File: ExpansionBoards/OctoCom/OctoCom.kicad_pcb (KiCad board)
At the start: 4 copper layers, 106.7 x 83.8 mm, 101 parts, among them J1 Conn_02x10_Odd_Even, J10 Conn_02x02_Odd_Even, J11 Conn_02x02_Odd_Even, J12 Conn_02x02_Odd_Even, J13 Conn_02x02_Odd_Even, J14 DPD-09-11-B3, J15 Conn_02x02_Odd_Even, J16 Conn_02x02_Odd_Even, J17 Conn_02x02_Odd_Even, J18 Conn_02x02_Odd_Even, J19 Conn_02x02_Odd_Even, J2 Conn_02x20_Odd_Even, J20 Conn_02x02_Odd_Even, J21 DPD-09-11-B3, J22 Conn_02x02_Odd_Even, J23 Conn_02x02_Odd_Even, J24 Conn_02x02_Odd_Even, J25 Conn_02x02_Odd_Even, J26 Conn_02x02_Odd_Even, J27 Conn_02x02_Odd_Even, J28 DPD-09-11-B3, J29 Conn_02x02_Odd_Even, J30 Conn_02x02_Odd_Even, J31 Conn_02x02_Odd_Even, J32 Conn_02x04_Odd_Even, J33 4-171826-4, J34 Conn_02x03_Odd_Even, J4 DPD-09-11-B3, J5 Conn_02x02_Odd_Even, J6 Conn_02x02_Odd_Even, J7 Conn_02x02_Odd_Even, J8 Conn_02x02_Odd_Even, J9 Conn_02x02_Odd_Even, U1 ST16C554D, U10 SP3243EEY, U11 SP3243EEY, U12 74LS74, U14 SP3243EEY, U16 74LS00, U2 74LS139, U3 74HCT138, U4 SP3243EEY, U5 SP3243EEY, U6 SP3243EEY, U7 SP3243EEY, U8 SP3243EEY, U9 ST16C554D, X1 1.8432M, X1-ALT 1.8432M

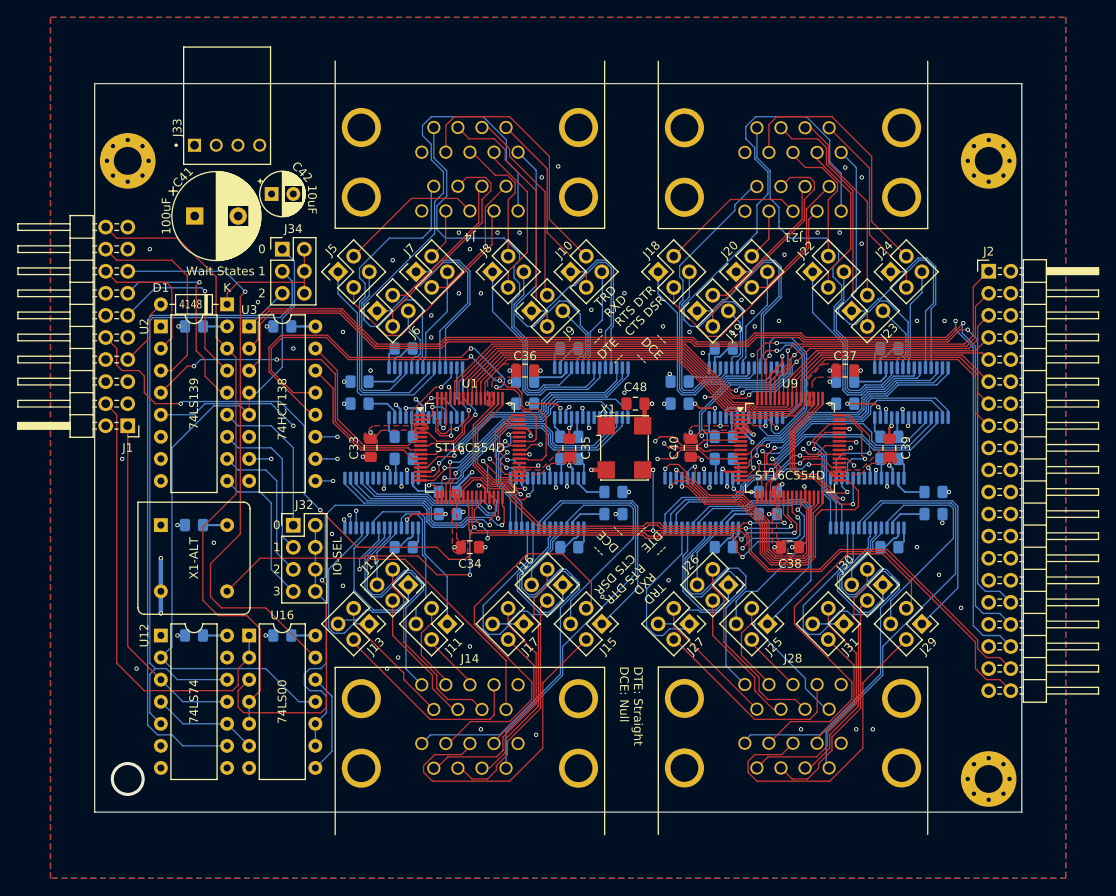
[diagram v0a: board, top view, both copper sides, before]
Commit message: rework octocom logic to use 22V10 for speed
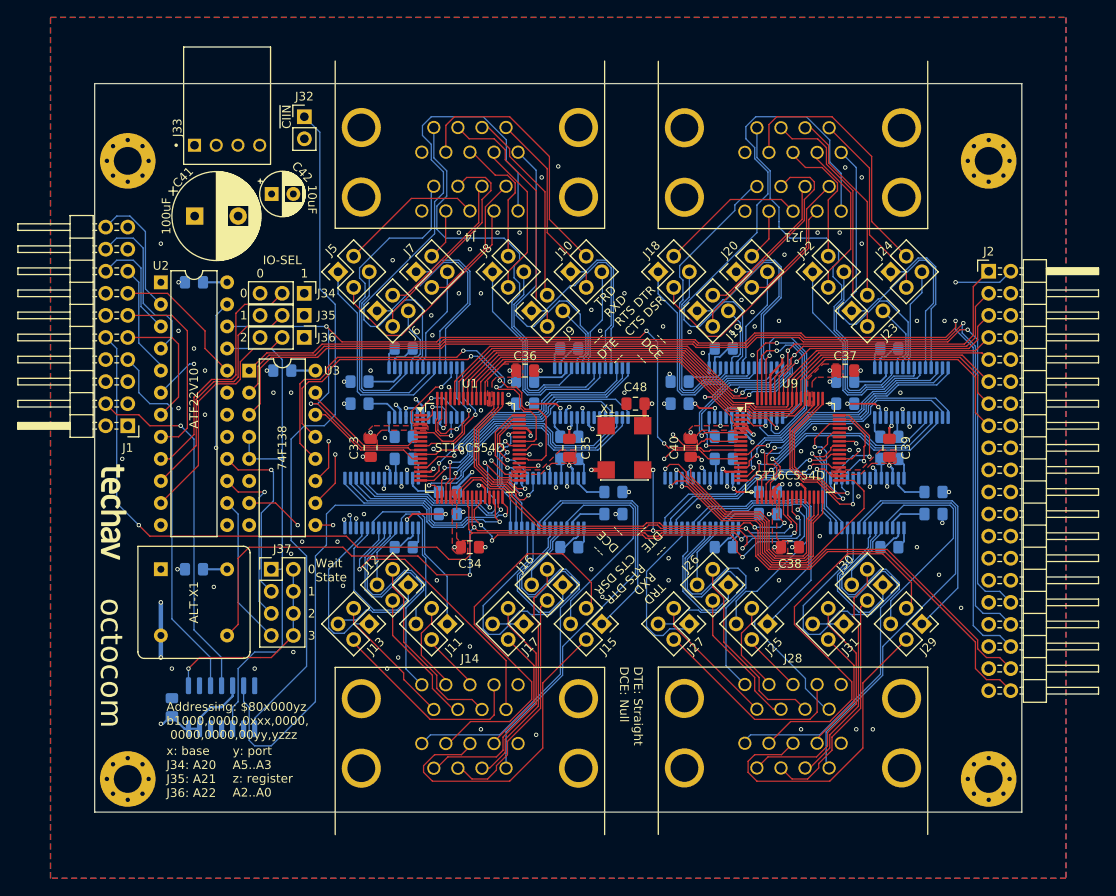
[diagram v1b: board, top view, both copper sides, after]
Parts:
- removed C43: 33n, Capacitor_SMD:C_0805_2012Metric_Pad1.18x1.45mm_HandSolder
- removed D1: 4148, Diode_THT:D_DO-35_SOD27_P7.62mm_Horizontal
- removed U12: 74LS74, Package_DIP:DIP-14_W7.62mm
- removed U16: 74LS00, Package_DIP:DIP-14_W7.62mm
- removed X1-ALT: 1.8432M, Oscillator:Oscillator_DIP-8
- added ALT-X1: 1.8432M, Oscillator:Oscillator_DIP-8, F.Cu at (78.7, 96.5)
- added H1: M3, MountingHole:MountingHole_3.2mm_M3_Pad_Via, F.Cu at (74.9, 120.7)
- added J35: Conn_01x03, Connector_PinHeader_2.54mm:PinHeader_1x03_P2.54mm_Vertical, F.Cu at (95.2, 67.3)
- added J36: Conn_01x03, Connector_PinHeader_2.54mm:PinHeader_1x03_P2.54mm_Vertical, F.Cu at (95.2, 69.8)
- added J37: Conn_02x04_Odd_Even, Connector_PinHeader_2.54mm:PinHeader_2x04_P2.54mm_Vertical, F.Cu at (91.4, 96.5)
- added U13: SN74AHCT125, Package_SO:SO-14_3.9x8.65mm_P1.27mm, B.Cu at (85.7, 112.4)
- J32: value Conn_02x04_Odd_Even -> Conn_01x02; footprint Connector_PinHeader_2.54mm:PinHeader_2x04_P2.54mm_Vertical -> Connector_PinHeader_2.54mm:PinHeader_1x02_P2.54mm_Vertical
- J34: value Conn_02x03_Odd_Even -> Conn_01x03; footprint Connector_PinHeader_2.54mm:PinHeader_2x03_P2.54mm_Vertical -> Connector_PinHeader_2.54mm:PinHeader_1x03_P2.54mm_Vertical
- U2: value 74LS139 -> ATF22V10; footprint Package_DIP:DIP-16_W7.62mm -> Package_DIP:DIP-24_W7.62mm
- U3: value 74HCT138 -> 74F138
- moved J32 47.0 mm to (95.2, 44.5)
- moved C44 41.9 mm to (82.5, 63.5)
- moved C46 8.64 mm to (80.0, 112.4), turned to 90 degrees
- moved J34 5.67 mm to (95.2, 64.8), turned to -90 degrees
- moved C45 5.08 mm to (92.7, 73.7)
- moved C47 5.08 mm to (82.5, 96.5)
- moved U2 5.08 mm to (78.7, 63.5)
- moved U3 5.08 mm to (88.9, 73.7)
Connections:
- J32 pad 1: /~{IO-SEL0} -> /~{CPU-CIIN}
- J32 pad 2: Net-(J32-Pin_2) -> GND
- J34 pad 1: /~{IO-CE} -> VCC
- J34 pad 2: Net-(D1-K) -> /IOSEL0
- J34 pad 3: Net-(J34-Pin_3) -> GND
- U2 pad 1: GND -> /CPU-CLK
- U2 pad 10: /~{IO-SEL2} -> /IOSEL1
- U2 pad 11: /~{IO-SEL1} -> /IOSEL2
- U2 pad 12: /~{IO-SEL0} -> GND
- U2 pad 13: /CPU-A23 -> unconnected-(U2-~{OE}-Pad13)
- U2 pad 14: /CPU-A22 -> /~{1WS}
- U2 pad 15: /~{CPU-AS} -> /~{2WS}
- U2 pad 16: VCC -> /~{3WS}
- U2 pad 2: /CPU-R/~{W} -> /~{CPU-AS}
- U2 pad 3: /~{CPU-DS} -> /CPU-R/~{W}
- U2 pad 4: /~{IOWR} -> /~{CPU-DS}
- U2 pad 5: /~{IORD} -> /CPU-A31
- U2 pad 6: unconnected-(U2A-O2-Pad6) -> /CPU-A20
- U2 pad 7: unconnected-(U2A-O3-Pad7) -> /CPU-A21
- U2 pad 8: GND -> /CPU-A22
- U2 pad 9: /~{IO-SEL3} -> /IOSEL0
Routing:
- net /CPU-A20: track 0.00 -> 106.1 mm, vias 0 -> 2
- net /~{CPU-CIIN}: track 0.00 -> 78.5 mm
- net Net-(J34-Pin_3): track 77.7 -> 0.00 mm
- net Net-(J34-Pin_5): track 73.5 -> 0.00 mm
- net /~{CPU-AS}: track 74.2 -> 15.0 mm
- net /CPU-A31: track 66.2 -> 13.0 mm, vias 1 -> 0
- net /~{CPU-DSACK0}: track 7.93 -> 42.7 mm
- net Net-(J32-Pin_2): track 30.0 -> 0.00 mm
- net /IOSEL0: track 0.00 -> 28.5 mm
- net /IOSEL1: track 0.00 -> 27.8 mm
- net /IOSEL2: track 0.00 -> 27.4 mm
- net Net-(J37-Pin_2): track 0.00 -> 23.2 mm, vias 0 -> 1
- net /CPU-CLK: track 39.5 -> 18.1 mm
- net /~{3WS}: track 0.00 -> 20.7 mm, vias 0 -> 1
- net /~{2WS}: track 0.00 -> 19.7 mm, vias 0 -> 1
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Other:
- board text added: "Addressing: $80x000yz b1000,0000,0xxx,0000, 0000,0000,00yy,yzzz"
- board text added: "Wait State"
- board text added: "octocom"
- board text added: "x: base J34: A20 J35: A21 J36: A22"
- board text added: "y: port A5..A3"
- board text added: "z: register A2..A0"
- board text added: "~{CIIN}"
- board text removed: "Wait States"
